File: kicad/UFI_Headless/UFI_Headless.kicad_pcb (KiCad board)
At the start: 4 copper layers, 110 x 85 mm, 104 parts, among them J1 USB-C, J2 12V DC 5.5/2.1, J3 FDD_PWR, J4 SWD, J5 DBG_UART, J6 FDD_34PIN, J7 AMIGA_FDD, J8 IEC_HDR, SW1 RESET, SW2 BOOT, U1 USBLC6-2SC6, U10 74LVC14AD, U2 TPS54202DDC, U3 TPS2116DRL, U4 AP7361C-33E, U5 STM32H723ZGT6, U6 SN74LS07D, U7 SN74LS07D, U8 74LVC14AD, U9 SN74LS07D, Y1 25MHz CL=12pF

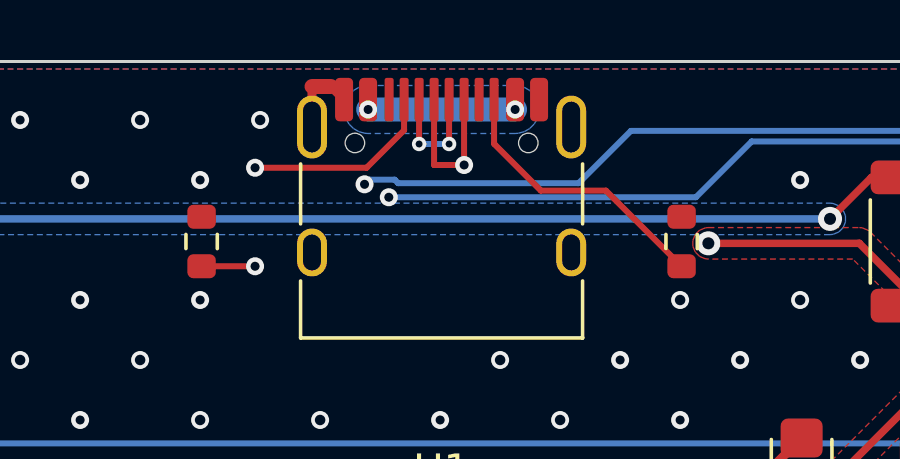
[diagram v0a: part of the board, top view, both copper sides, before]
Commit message: UFI Headless: no via-in-pad at USB-C, JLC rotation offsets + viewer checklist
- VBUS vias moved out of the J1 A4/A9 pads (0.5/0.25, inwards: the NPTH
  pegs sit right below the pads); CC2 re-routed left of the A9 via.
  Board-wide check: 0 vias touching SMD pads -> plain tented vias suffice.
- scripts/jlc_cpl.py: JLC CPL with kicad-jlcpcb-tools package rotation
  offsets and fertigung/JLC_Rotation_Check.md (pin-1 location of the 22
  polarised parts) for the JLC placement viewer.
DRC: 0 errors, 0 unconnected, parity clean.

Co-Authored-By: Claude Opus 5.5 <noreply@anthropic.com>
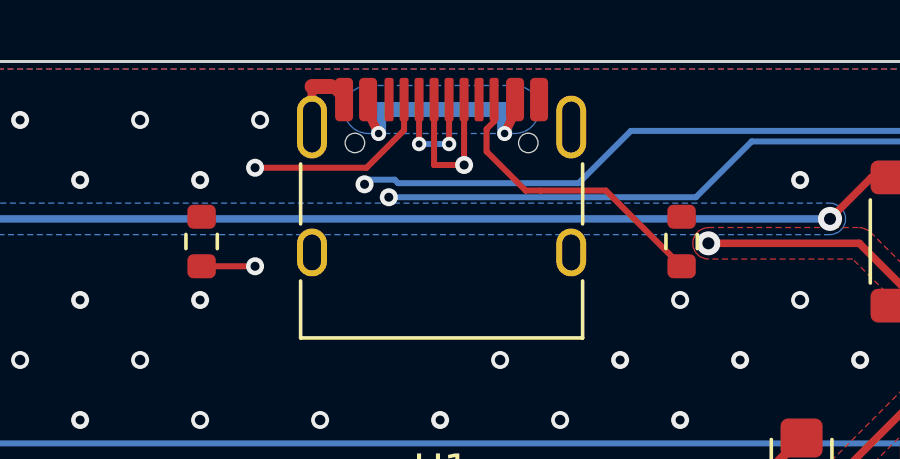
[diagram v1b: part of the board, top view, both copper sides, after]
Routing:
- net VBUS: track 52.2 -> 55.7 mm
- net /Power/CC2: track 9.41 -> 9.92 mm
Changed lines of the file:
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@@
 	)
 	(segment
+		(start 74.45 1.27)
+		(end 74.45 1.695)
+		(width 0.3)
+		(locked yes)
+		(layer "F.Cu")
+		(net "VBUS")
+	)
+	(segment
 		(start 84 15.45)
 		(end 83.45 16)
@@
 	)
 	(segment
+		(start 69.55 1.27)
+		(end 69.55 1.695)
+		(width 0.3)
+		(locked yes)
+		(layer "F.Cu")
+		(net "VBUS")
+	)
+	(segment
+		(start 69.55 1.695)
+		(end 69.9 2.4)
+		(width 0.3)
+		(locked yes)
+		(layer "F.Cu")
+		(net "VBUS")
+	)
+	(segment
 		(start 83.45 16)
 		(end 75.2137 16)
@@
 	)
 	(segment
-		(start 74.45 1.6)
-		(end 74.45 1.27)
-		(width 0.25)
+		(start 74.45 1.695)
+		(end 74.1 2.4)
+		(width 0.3)
+		(locked yes)
 		(layer "F.Cu")
 		(net "VBUS")
@@
 		(net "VBUS")
 	)
-	(segment
-		(start 69.55 1.6)
-		(end 69.55 1.27)
-		(width 0.25)
-		(layer "F.Cu")
-		(net "VBUS")
-	)
 	(via
-		(at 69.55 1.6)
-		(size 0.6)
-		(drill 0.3)
+		(at 69.9 2.4)
+		(size 0.5)
+		(drill 0.25)
 		(layers "F.Cu" "B.Cu")
 		(locked yes)
@@
 	)
 	(via
-		(at 74.45 1.6)
-		(size 0.6)
-		(drill 0.3)
+		(at 74.1 2.4)
+		(size 0.5)
+		(drill 0.25)
 		(layers "F.Cu" "B.Cu")
 		(locked yes)
@@
 	)
 	(segment
-		(start 69.55 1.6)
-		(end 74.45 1.6)
-		(width 0.8)
+		(start 69.9 1.6)
+		(end 74.1 1.6)
+		(width 0.5)
+		(locked yes)
+		(layer "B.Cu")
+		(net "VBUS")
+	)
+	(segment
+		(start 74.1 1.6)
+		(end 74.1 2.4)
+		(width 0.5)
+		(locked yes)
+		(layer "B.Cu")
+		(net "VBUS")
+	)
+	(segment
+		(start 69.9 2.4)
+		(end 69.9 1.6)
+		(width 0.5)
 		(locked yes)
 		(layer "B.Cu")
@@
 	)
 	(segment
+		(start 74.1 2.4)
+		(end 74.45 1.6)
+		(width 0.5)
+		(locked yes)
+		(layer "In2.Cu")
+		(net "VBUS")
+	)
+	(segment
 		(start 80.4288 5.5977)
 		(end 80.8917 6.0606)
@@
 	)
 	(segment
+		(start 73.75 2)
+		(end 73.5 2.25)
+		(width 0.2)
+		(locked yes)
+		(layer "F.Cu")
+		(net "/Power/CC2")
+	)
+	(segment
+		(start 73.5 3)
+		(end 74.803 4.303)
+		(width 0.2)
+		(locked yes)
+		(layer "F.Cu")
+		(net "/Power/CC2")
+	)
+	(segment
 		(start 73.75 1.27)
-		(end 73.75 2.7441)
+		(end 73.75 2)
 		(width 0.2)
+		(locked yes)
 		(layer "F.Cu")
 		(net "/Power/CC2")
 	)
 	(segment
-		(start 73.75 2.7441)
-		(end 75.3094 4.3035)
+		(start 73.5 2.25)
+		(end 73.5 3)
 		(width 0.2)
+		(locked yes)
 		(layer "F.Cu")
 		(net "/Power/CC2")
@@
 		(layer "F.Cu")
 		(net "/Power/CC2")
+	)
+	(segment
+		(start 74.803 4.303)
+		(end 75.309 4.303)
+		(width 0.2)
+		(locked yes)
+		(layer "F.Cu")
+		(net "/Power/CC2")

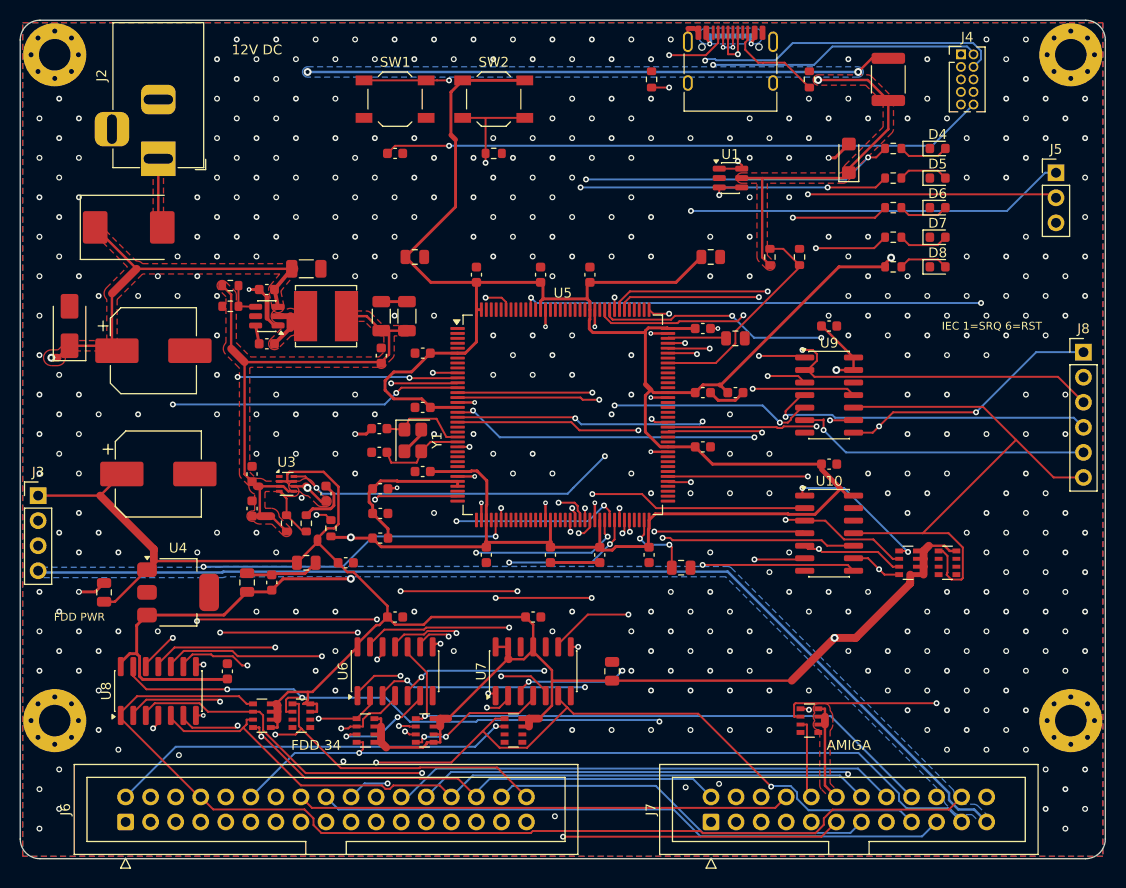
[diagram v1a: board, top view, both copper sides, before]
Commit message: UFI Headless v0.2: 8 MB PSRAM, ESD, drive polyfuses, test points
Schematic (new parts get fixed references above the v0.1 maxima, so all
existing references and PCB links stay unchanged):
- U11 APS6404L 8 MB QSPI PSRAM on OCTOSPIM P1 (PB2/PB10/PD11/PD12/PB13/
  PD13), C46, CE# pull-up R16
- D9-D11 ESDA6V1-5SC6 on the 13 Amiga J7 bus lines + MOTOR_A, D12 on IEC
- F2/F3 polyfuses: drive supplies FDD_5V/FDD_12V for J3 and J7 pins 12/23
- TP1-TP6 (3V3, 5V, 12V, GND, RDATA, INDEX), excluded from BOM/CPL
Layout (incremental ECO on the reviewed board):
- scripts/add_parts.py: re-net pads, collision-aware placement, rip up only
  what is in the way; make_pcb.sh 'eco' step
- fixes found on the way: supply pours ran after finish_pcb and left GND
  islands (LDO U4 ground!) without vias -> order swapped, GND pour check
  per net; island/dogbone vias never inside pads; manual_routes no longer
  re-applies the D+ fallback; pipeline filters robust against interleaved
  SWIG noise under pipefail
- DRC rule for the intentional J6/J7 silk overhang instead of warnings;
  netclasses cover the new drive supply nets
DRC: 0 errors, 0 warnings, 0 unconnected, parity clean, no via-in-pad.

Co-Authored-By: Claude Opus 5.5 <noreply@anthropic.com>
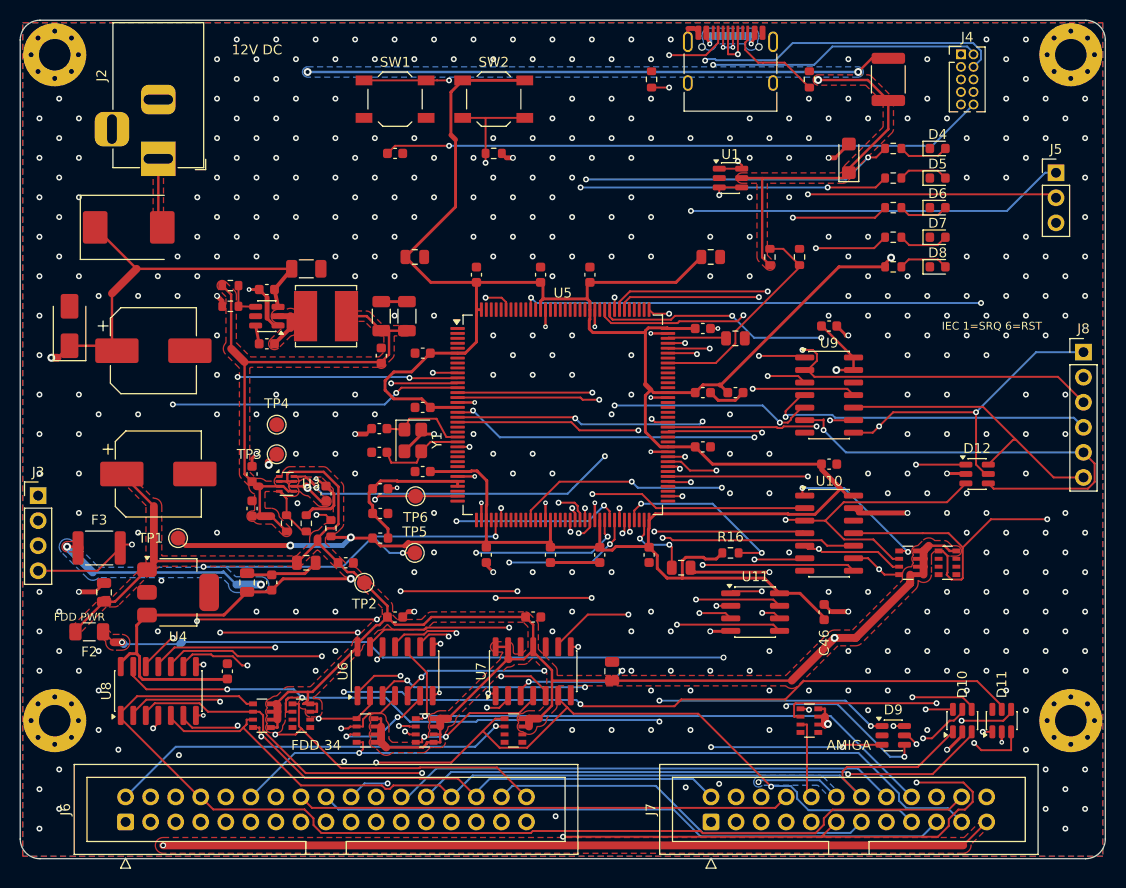
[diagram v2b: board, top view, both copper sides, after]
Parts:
- added C46: 100nF, Capacitor_SMD:C_0603_1608Metric, F.Cu at (81.5, 60.0)
- added D10: ESDA6V1-5SC6, Package_TO_SOT_SMD:SOT-23-6, F.Cu at (95.5, 71.0)
- added D11: ESDA6V1-5SC6, Package_TO_SOT_SMD:SOT-23-6, F.Cu at (99.5, 71.0)
- added D12: ESDA6V1-5SC6, Package_TO_SOT_SMD:SOT-23-6, F.Cu at (97.0, 46.0)
- added D9: ESDA6V1-5SC6, Package_TO_SOT_SMD:SOT-23-6, F.Cu at (88.5, 72.5)
- added F2: 1.1A hold 6V, Fuse:Fuse_1206_3216Metric, F.Cu at (7.00, 62.0)
- added F3: 1.1A hold 24V, Fuse:Fuse_1812_4532Metric, F.Cu at (8.00, 53.5)
- added R16: 10k, Resistor_SMD:R_0603_1608Metric, F.Cu at (72.0, 54.0)
- added TP1: TP_3V3, TestPoint:TestPoint_Pad_D1.5mm, F.Cu at (16.0, 52.5)
- added TP2: TP_5V, TestPoint:TestPoint_Pad_D1.5mm, F.Cu at (34.9, 57.0)
- added TP3: TP_12V, TestPoint:TestPoint_Pad_D1.5mm, F.Cu at (26.0, 44.0)
- added TP4: TP_GND, TestPoint:TestPoint_Pad_D1.5mm, F.Cu at (26.0, 41.0)
- added TP5: TP_RDATA, TestPoint:TestPoint_Pad_D1.5mm, F.Cu at (40.0, 54.0)
- added TP6: TP_INDEX, TestPoint:TestPoint_Pad_D1.5mm, F.Cu at (40.1, 48.2)
- added U11: APS6404L-3SQR-SN, Package_SO:SOIC-8_3.9x4.9mm_P1.27mm, F.Cu at (74.5, 60.0)
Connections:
- J3 pad 1: +5V -> FDD_5V
- J3 pad 4: +12V -> FDD_12V
- J7 pad 12: +5V -> FDD_5V
- J7 pad 23: +12V -> FDD_12V
- U5 pad 48: unconnected-(U5-PB2-Pad48) -> /MCU_Core/PSRAM_CLK
- U5 pad 69: unconnected-(U5-PB10-Pad69) -> /MCU_Core/PSRAM_CS
- U5 pad 74: unconnected-(U5-PB13-Pad74) -> /MCU_Core/PSRAM_IO2
- U5 pad 80: unconnected-(U5-PD11-Pad80) -> /MCU_Core/PSRAM_IO0
- U5 pad 81: unconnected-(U5-PD12-Pad81) -> /MCU_Core/PSRAM_IO1
- U5 pad 82: unconnected-(U5-PD13-Pad82) -> /MCU_Core/PSRAM_IO3
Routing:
- net FDD_12V: track 0.00 -> 126.9 mm, vias 0 -> 2
- net FDD_5V: track 0.00 -> 105.5 mm, vias 0 -> 3
- net FD_MOTOR_A: track 19.4 -> 93.0 mm, vias 1 -> 3
- net +12V: track 171.7 -> 98.5 mm, vias 1 -> 4
- net +3V3: track 313.4 -> 359.7 mm, vias 3 -> 4
- net /MCU_Core/PSRAM_CLK: track 0.00 -> 38.2 mm, vias 0 -> 3
- net GND: track 63.0 -> 100.5 mm, vias 434 -> 408
- net FD_DSKCHG: track 87.5 -> 117.2 mm, vias 3 -> 5
- net /MCU_Core/PSRAM_IO0: track 0.00 -> 27.9 mm, vias 0 -> 2
- net FD_READY: track 72.3 -> 100.2 mm, vias 3 -> 5
- net /MCU_Core/PSRAM_IO3: track 0.00 -> 25.7 mm, vias 0 -> 2
- net /MCU_Core/PSRAM_CS: track 0.00 -> 25.7 mm, vias 0 -> 3
- net FD_MOTOR_B: track 66.2 -> 90.9 mm, vias 1 -> 3
- net FD_RDATA: track 67.0 -> 89.5 mm, vias 2 -> 4
- net /MCU_Core/PSRAM_IO1: track 0.00 -> 20.5 mm, vias 0 -> 2
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- added copper zone on F.Cu, net FDD_12V
- added copper zone on In2.Cu, net FDD_12V
- added copper zone on B.Cu, net FDD_5V
- added copper zone on F.Cu, net FDD_5V
- added copper zone on In2.Cu, net FDD_5V

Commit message: UFI Headless v0.3: USB-C source current detection
- schematic: CC1/CC2 (Rd 5.1k) also to PA0/PA3 (ADC1 INP16/INP15); ECO
  routed on the reviewed board, DRC 0 errors / 0 warnings, parity clean
- firmware: USB_POWER (0x19) measures CC voltages, reports the allowed
  source current (0.5 / 1.5 / 3 A per Type-C vRd ranges)
- host tool: ufi usb-power
- manual_routes: D+ fallback skipped when any D+ via is near its start
  (Freerouting's own via sits 0.25 mm away; it was re-added every run)
- README: CC pins, Atari SIO option on existing UART pins (PD1/PF6/PD0)

Co-Authored-By: Claude Opus 5.5 <noreply@anthropic.com>
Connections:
- J1 pad A5: /Power/CC1 -> CC1
- J1 pad B5: /Power/CC2 -> CC2
- R1 pad 1: /Power/CC1 -> CC1
- R2 pad 1: /Power/CC2 -> CC2
- U5 pad 34: unconnected-(U5-PA0-Pad34) -> CC1
- U5 pad 37: unconnected-(U5-PA3-Pad37) -> CC2
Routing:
- net CC2: track 0.00 -> 80.8 mm, vias 0 -> 2
- net CC1: track 0.00 -> 63.5 mm, vias 0 -> 3
- net /Power/CC1: track 11.6 -> 0.00 mm, vias 2 -> 0
- net /Power/CC2: track 9.92 -> 0.00 mm
- net GND: track 100.5 -> 102.0 mm, vias 408 -> 401
